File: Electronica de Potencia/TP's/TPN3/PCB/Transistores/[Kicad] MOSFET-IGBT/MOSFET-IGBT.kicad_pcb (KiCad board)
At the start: 2 copper layers, 70.9 x 52.3 mm, 20 parts, among them J1 Vin, J2 PWM_IN, Q1 FGPF7N60RUFD, Q2 IRF840, T1 50:50

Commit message: Arreglo placa de potencia
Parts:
- JP1: value IGBT -> Jumper_NC_Small
- JP2: value MOSFET O IGBT -> Jumper_NC_Dual
- JP3: value MOSFET -> Jumper_NC_Small
- TP3: value TP_VDS -> TP_VCE_VDS
- moved D1 78.2 mm to (159.0, 92.1), turned to 180 degrees
- moved D2 73.7 mm to (151.4, 87.9), turned to 0 degrees
- moved JP1 70.5 mm to (167.6, 87.8)
- moved JP2 69.9 mm to (168.1, 97.8)
- moved G1 68.5 mm to (121.2, 83.7)
- moved J2 68.4 mm to (123.1, 92.9)
- moved JP3 67.9 mm to (167.5, 82.8)
- moved TP3 67.2 mm to (171.6, 71.4)
- moved J1 67.0 mm to (119.2, 73.4)
- moved Q2 67.0 mm to (174.7, 77.8)
- moved R2 67.0 mm to (119.7, 113.3)
- moved HS1 67.0 mm to (198.2, 70.4)
- moved HS2 67.0 mm to (198.6, 92.7)
- moved Q1 67.0 mm to (175.2, 100.0)
- moved TP2 66.8 mm to (153.3, 71.5)
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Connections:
- J2 pad 1: /PWM_A -> /PWM_B
- J2 pad 3: /PWM_B -> /PWM_A
- Q1 pad 3: GND -> Earth
- Q2 pad 1: Net-(JP3-Pad2) -> Net-(JP2-Pad3)
- Q2 pad 2: Net-(JP2-Pad3) -> Net-(JP3-Pad2)
- Q2 pad 3: GND -> Earth
- R1 pad 2: GND -> Earth
- T1 pad : /PWM_A -> Net-(JP1-Pad1)
- T1 pad 3: GND -> Earth
- TP2 pad 1: GND -> Earth
- TP3 pad 1: Net-(JP2-Pad3) -> Net-(JP2-Pad2)
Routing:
- net GND: track 5.84 -> 109.6 mm, vias 2 -> 0
- net Earth: track 0.00 -> 96.4 mm, vias 0 -> 2
- net Net-(JP2-Pad2): track 16.6 -> 83.1 mm
- net Net-(JP1-Pad1): track 58.9 -> 93.9 mm
- net Net-(JP2-Pad3): track 81.3 -> 53.8 mm
- net /PWM_B: track 52.6 -> 63.2 mm
- net +15V: track 100.5 -> 109.3 mm
- net /PWM_A: track 52.9 -> 48.6 mm
- net Net-(JP1-Pad2): track 12.7 -> 16.0 mm
- net Net-(JP2-Pad1): track 9.40 -> 12.0 mm
- net Net-(JP3-Pad2): track 9.26 -> 7.19 mm

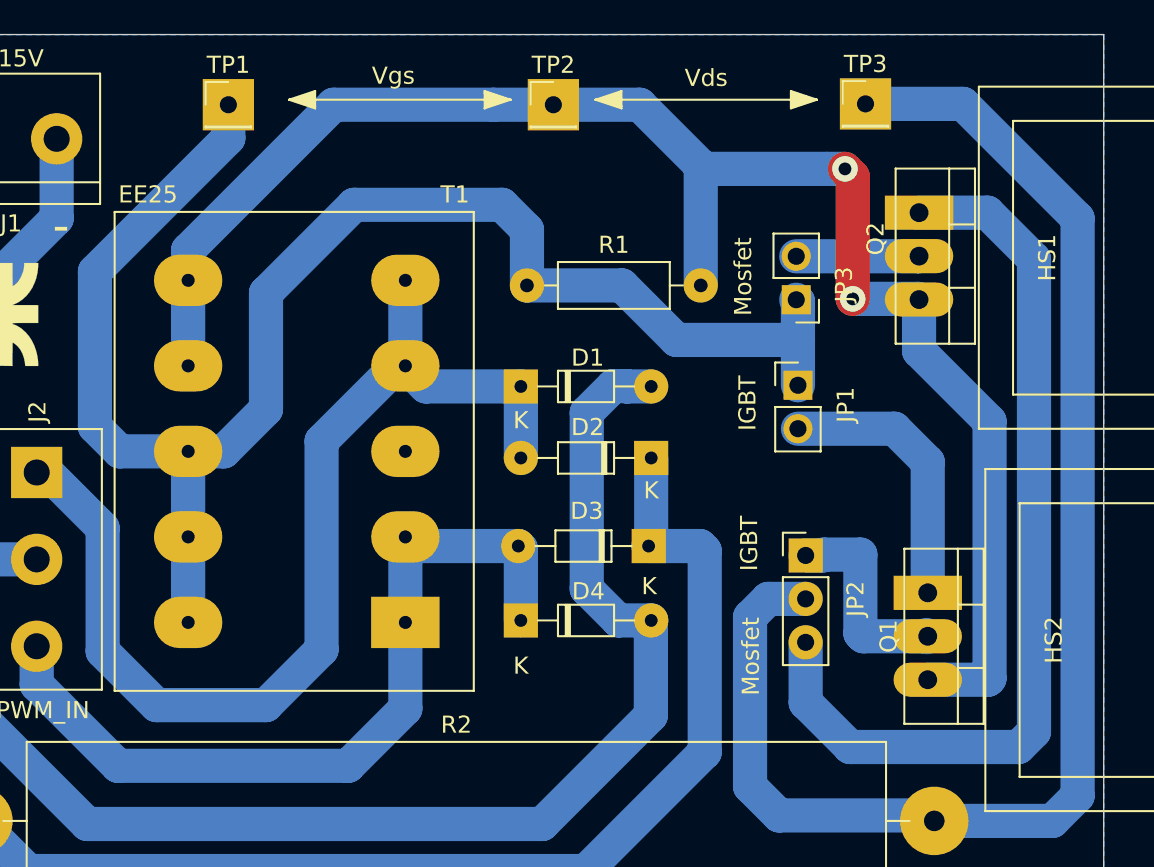
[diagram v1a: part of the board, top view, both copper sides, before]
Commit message: Arreglo placa BJT potencia
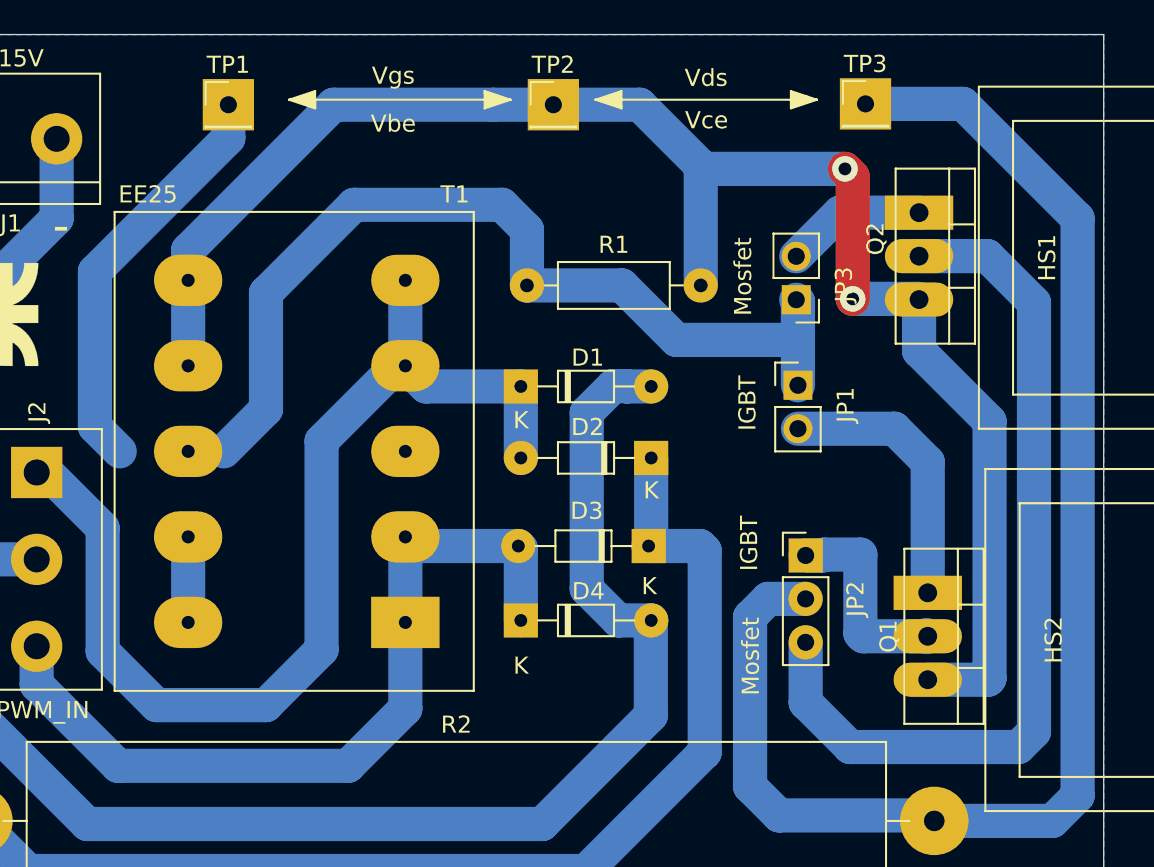
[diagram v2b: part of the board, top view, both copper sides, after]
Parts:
- JP1: value Jumper_NC_Small -> IGBT_Jumper
- JP2: value Jumper_NC_Dual -> Jumper_Dual
- JP3: value Jumper_NC_Small -> Mosfet_Jumper
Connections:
- T1 pad : Net-(JP1-Pad1) -> (no net)
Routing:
- net Net-(JP1-Pad1): track 93.9 -> 82.8 mm
- net Net-(JP2-Pad3): track 53.8 -> 51.2 mm
- net Net-(JP3-Pad2): track 7.19 -> 8.24 mm
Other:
- board text added: "Vbe"
- board text added: "Vce"
